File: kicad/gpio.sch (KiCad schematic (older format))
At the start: 11 parts

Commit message: usb interface changed by emu_interface
I've cleaned all the jtag interface, so the only things that go out is
jtag HOT and rx/tx isolated. I left the isolator for rx/tx cose I'm
planning to add rs485 using the same isolator and regulator, if not, I'd
clean these IC's also
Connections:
- net labels added: VDD3V3
- net labels removed: VDD
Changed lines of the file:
@@
 EESchema Schematic File Version 4
-LIBS:servo-cache
 EELAYER 26 0
 EELAYER END
 $Descr B 17000 11000
 encoding utf-8
-Sheet 4 7
+Sheet 3 6
 Title "gpio"
 Date "25 10 2019"
@@
 MCU_GPIO147
 $Comp
-L servo:VDD #PWR0409
+L servo:VDD3V3 #PWR0409
 U 1 1 5DB39007
 P 8050 1700
+AR Path="/5DB39007" Ref="#PWR0409"  Part="1"
+AR Path="/5DE49152/5DB39007" Ref="#PWR0409"  Part="1"
 F 0 "#PWR0409" H 8067 1909 20  0000 C CNN
-F 1 "VDD" H 8067 1857 30  0000 C CNN
+F 1 "VDD3V3" H 8067 1857 30  0000 C CNN
 F 2 "" H 8050 1700 70  0000 C CNN
 F 3 "" H 8050 1700 70  0000 C CNN
@@
 F 1 "~" H 3000 5100 50  0001 C CNN
 F 2 "" H 3000 5100 50  0001 C CNN
-F 3 "" H 3000 5100 50  0001 C CNN
+F 3 "../doc/datasheets/tms320f28388d_datasheet.pdf" H 3000 5100 50  0001 C CNN
 F 4 "TMS320F28388DZWTS" V 1400 2000 60  0001 C CNN "PartNumber"
 	1    3000 5100

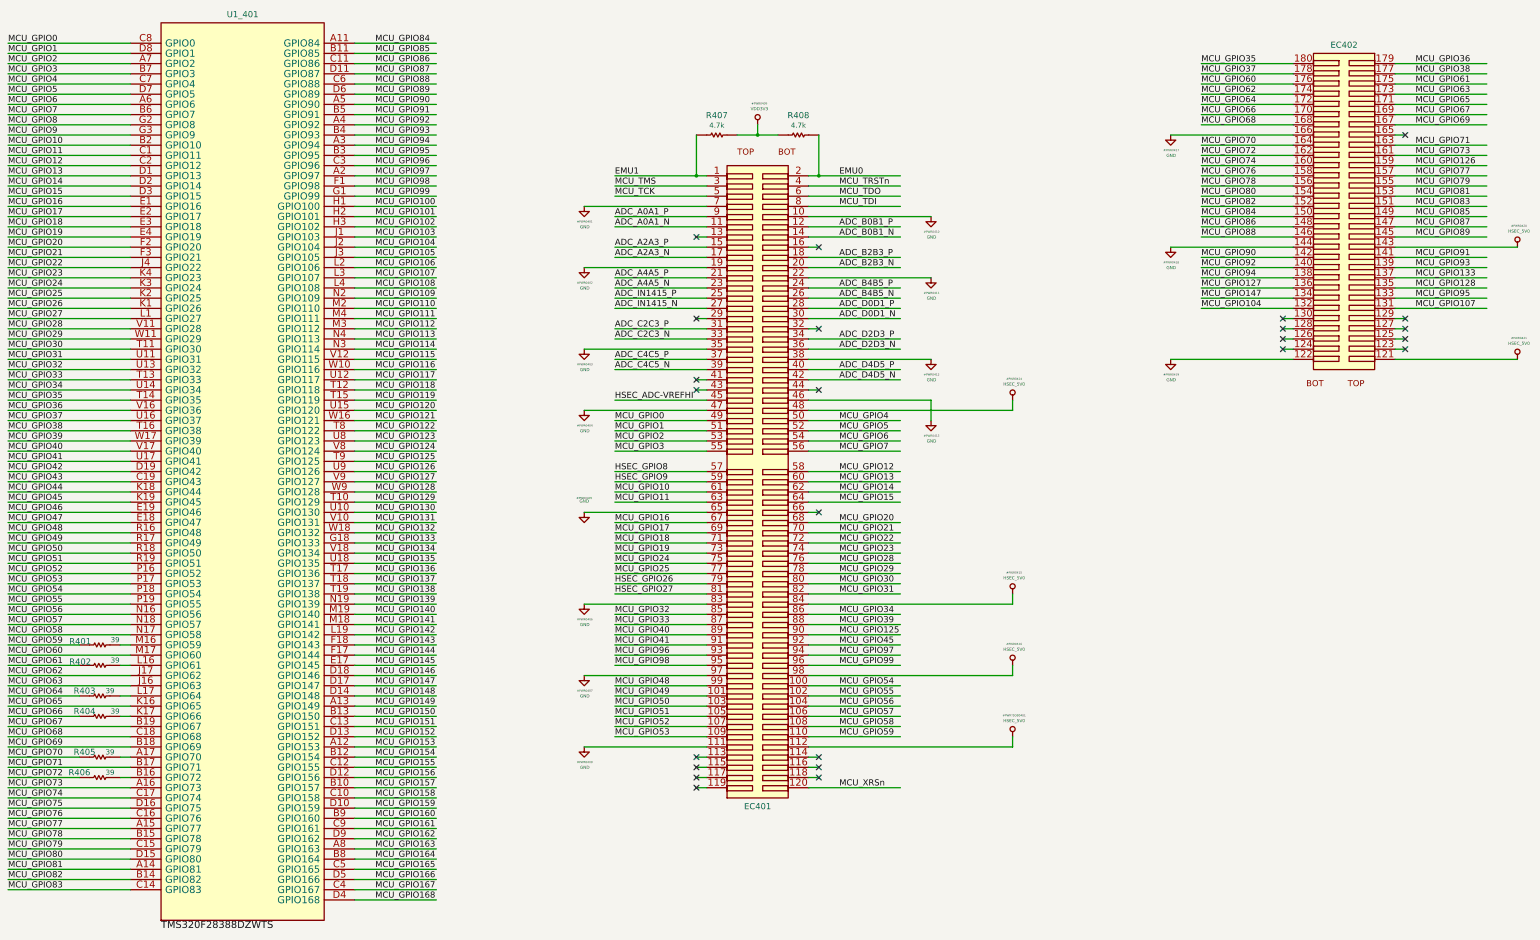
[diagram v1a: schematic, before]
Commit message: power.sch added with new power 1V2, 3V3, an so global labels
I've added the power schematic and try to ojin the power label as 3V3,
VDD_3V3 an so.. keep going
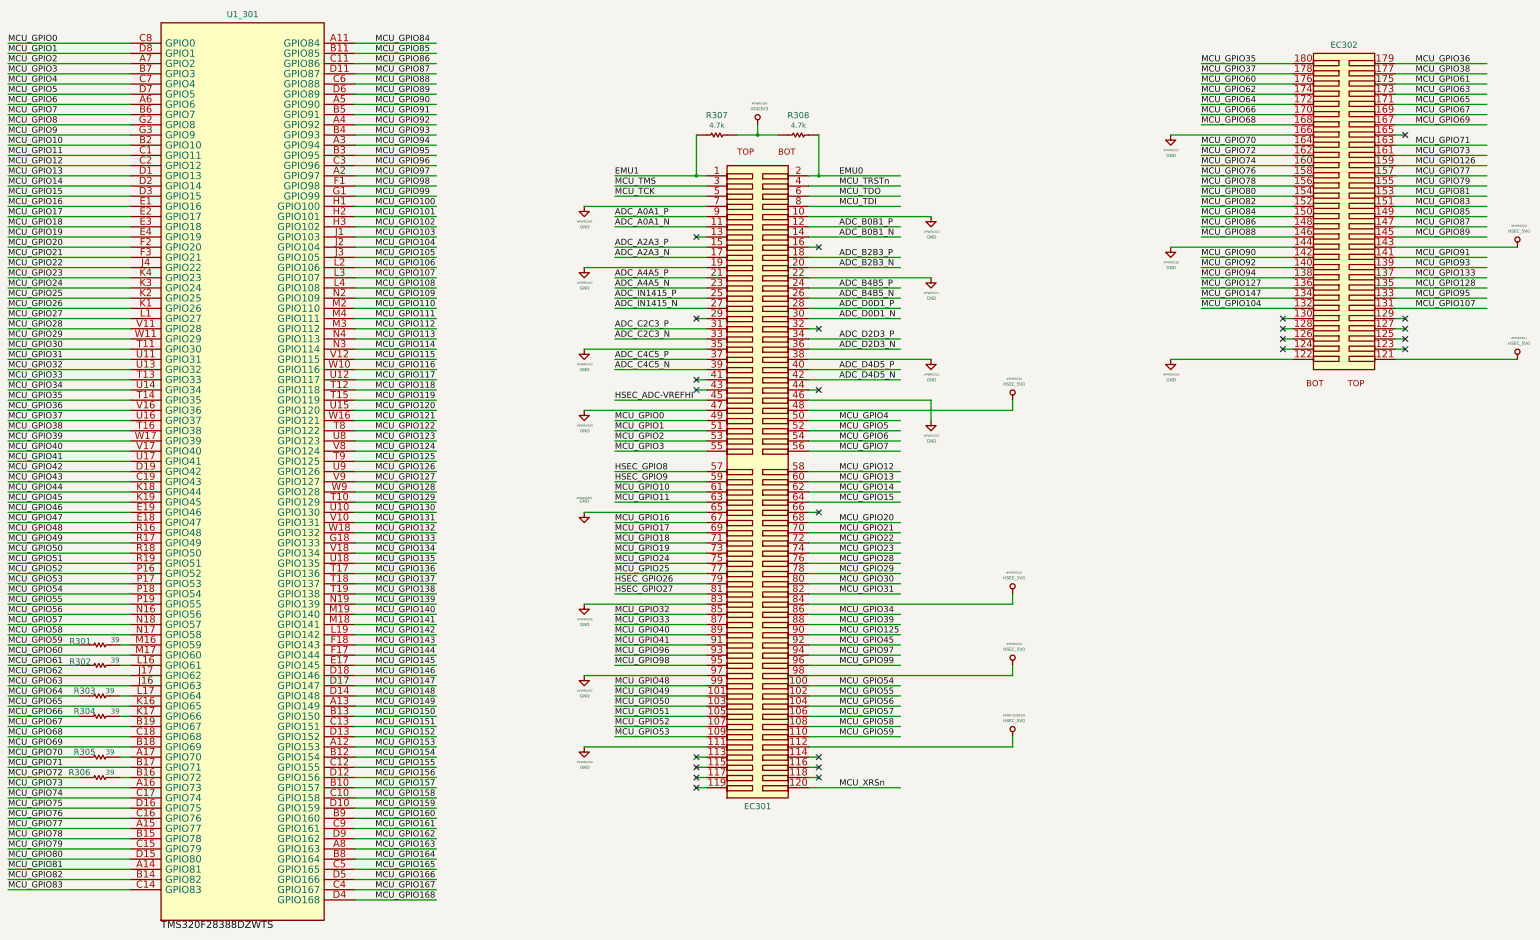
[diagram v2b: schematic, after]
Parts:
- renumbered EC401 to EC301, EC402 to EC302, R401 to R301, R402 to R302, R403 to R303, R404 to R304, R405 to R305, R406 to R306, R407 to R307, R408 to R308, U1_401 to U1_301
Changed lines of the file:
@@
 EESchema Schematic File Version 4
+LIBS:servo-cache
 EELAYER 26 0
 EELAYER END
 $Descr B 17000 11000
 encoding utf-8
-Sheet 3 6
+Sheet 3 7
 Title "gpio"
 Date "25 10 2019"
@@
 $EndDescr
 $Comp
-L servo:GND #PWR0401
+L servo:GND #PWR0301
 U 1 1 5DB3901C
 P 6350 2500
-F 0 "#PWR0401" H 6355 2351 20  0000 C CNN
+F 0 "#PWR0301" H 6355 2351 20  0000 C CNN
 F 1 "GND" H 6355 2299 30  0000 C CNN
 F 2 "" H 6350 2500 70  0000 C CNN
@@
 $EndComp
 $Comp
-L servo:GND #PWR0402
+L servo:GND #PWR0302
 U 1 1 5DB3901B
 P 6350 3100
-F 0 "#PWR0402" H 6355 2951 20  0000 C CNN
+F 0 "#PWR0302" H 6355 2951 20  0000 C CNN
 F 1 "GND" H 6355 2899 30  0000 C CNN
 F 2 "" H 6350 3100 70  0000 C CNN
@@
 $EndComp
 $Comp
-L servo:GND #PWR0403
+L servo:GND #PWR0303
 U 1 1 5DB3901A
 P 6350 3900
-F 0 "#PWR0403" H 6355 3751 20  0000 C CNN
+F 0 "#PWR0303" H 6355 3751 20  0000 C CNN
 F 1 "GND" H 6355 3699 30  0000 C CNN
 F 2 "" H 6350 3900 70  0000 C CNN
@@
 $EndComp
 $Comp
-L servo:GND #PWR0404
+L servo:GND #PWR0304
 U 1 1 5DB39019
 P 6350 4500
-F 0 "#PWR0404" H 6355 4351 20  0000 C CNN
+F 0 "#PWR0304" H 6355 4351 20  0000 C CNN
 F 1 "GND" H 6355 4299 30  0000 C CNN
 F 2 "" H 6350 4500 70  0000 C CNN
@@
 $EndComp
 $Comp
-L servo:GND #PWR0405
+L servo:GND #PWR0305
 U 1 1 5DB39018
 P 6350 5500
-F 0 "#PWR0405" H 6350 5640 20  0000 C CNN
+F 0 "#PWR0305" H 6350 5640 20  0000 C CNN
 F 1 "GND" H 6350 5610 30  0000 C CNN
 F 2 "" H 6350 5500 70  0000 C CNN
@@
 $EndComp
 $Comp
-L servo:GND #PWR0406
+L servo:GND #PWR0306
 U 1 1 5DB39017
 P 6350 6400
-F 0 "#PWR0406" H 6355 6251 20  0000 C CNN
+F 0 "#PWR0306" H 6355 6251 20  0000 C CNN
 F 1 "GND" H 6355 6199 30  0000 C CNN
 F 2 "" H 6350 6400 70  0000 C CNN
@@
 $EndComp
 $Comp
-L servo:GND #PWR0407
+L servo:GND #PWR0307
 U 1 1 5DB39016
 P 6350 7100
-F 0 "#PWR0407" H 6355 6951 20  0000 C CNN
+F 0 "#PWR0307" H 6355 6951 20  0000 C CNN
 F 1 "GND" H 6355 6899 30  0000 C CNN
 F 2 "" H 6350 7100 70  0000 C CNN
@@
 $EndComp
 $Comp
-L servo:GND #PWR0408
+L servo:GND #PWR0308
 U 1 1 5DB39015
 P 6350 7800
-F 0 "#PWR0408" H 6355 7651 20  0000 C CNN
+F 0 "#PWR0308" H 6355 7651 20  0000 C CNN
 F 1 "GND" H 6355 7599 30  0000 C CNN
 F 2 "" H 6350 7800 70  0000 C CNN
@@
 $EndComp
 $Comp
-L servo:GND #PWR0410
+L servo:GND #PWR0310
 U 1 1 5DB39014
 P 9750 2600
-F 0 "#PWR0410" H 9755 2451 20  0000 C CNN
+F 0 "#PWR0310" H 9755 2451 20  0000 C CNN
 F 1 "GND" H 9755 2399 30  0000 C CNN
 F 2 "" H 9750 2600 70  0000 C CNN
@@
 $EndComp
 $Comp
-L servo:GND #PWR0411
+L servo:GND #PWR0311
 U 1 1 5DB39013
 P 9750 3200
-F 0 "#PWR0411" H 9755 3051 20  0000 C CNN
+F 0 "#PWR0311" H 9755 3051 20  0000 C CNN
 F 1 "GND" H 9755 2999 30  0000 C CNN
 F 2 "" H 9750 3200 70  0000 C CNN
@@
 $EndComp
 $Comp
-L servo:GND #PWR0412
+L servo:GND #PWR0312
 U 1 1 5DB39012
 P 9750 4000
-F 0 "#PWR0412" H 9755 3851 20  0000 C CNN
+F 0 "#PWR0312" H 9755 3851 20  0000 C CNN
 F 1 "GND" H 9755 3799 30  0000 C CNN
 F 2 "" H 9750 4000 70  0000 C CNN
@@
 $EndComp
 $Comp
-L servo:GND #PWR0413
+L servo:GND #PWR0313
 U 1 1 5DB39011
 P 9750 4600
-F 0 "#PWR0413" H 9755 4451 20  0000 C CNN
+F 0 "#PWR0313" H 9755 4451 20  0000 C CNN
 F 1 "GND" H 9755 4399 30  0000 C CNN
 F 2 "" H 9750 4600 70  0000 C CNN
@@
 MCU_GPIO9
 $Comp
-L servo:GND #PWR0417
+L servo:GND #PWR0317
 U 1 1 5DB39010
 P 12100 1800
-F 0 "#PWR0417" H 12105 1651 20  0000 C CNN
+F 0 "#PWR0317" H 12105 1651 20  0000 C CNN
 F 1 "GND" H 12105 1599 30  0000 C CNN
 F 2 "" H 12100 1800 70  0000 C CNN
@@
 $EndComp
 $Comp
-L servo:GND #PWR0418
+L servo:GND #PWR0318
 U 1 1 5DB3900F
 P 12100 2900
-F 0 "#PWR0418" H 12105 2751 20  0000 C CNN
+F 0 "#PWR0318" H 12105 2751 20  0000 C CNN
 F 1 "GND" H 12105 2699 30  0000 C CNN
 F 2 "" H 12100 2900 70  0000 C CNN
@@
 $EndComp
 $Comp
-L servo:GND #PWR0419
+L servo:GND #PWR0319
 U 1 1 5DB3900E
 P 12100 4000
-F 0 "#PWR0419" H 12105 3851 20  0000 C CNN
+F 0 "#PWR0319" H 12105 3851 20  0000 C CNN
 F 1 "GND" H 12105 3799 30  0000 C CNN
 F 2 "" H 12100 4000 70  0000 C CNN
@@
 	15500 2900 14300 2900
 $Comp
-L servo:HSEC_5V0 #PWR0420
+L servo:HSEC_5V0 #PWR0320
 U 1 1 5DB3900D
 P 15500 2900
-F 0 "#PWR0420" H 15515 3109 20  0000 C CNN
+F 0 "#PWR0320" H 15515 3109 20  0000 C CNN
 F 1 "HSEC_5V0" H 15515 3057 30  0000 C CNN
 F 2 "" H 15500 2900 70  0000 C CNN
@@
 $EndComp
 $Comp
-L servo:HSEC_5V0 #PWR0421
+L servo:HSEC_5V0 #PWR0321
 U 1 1 5DB3900C
 P 15500 4000
-F 0 "#PWR0421" H 15515 4209 20  0000 C CNN
+F 0 "#PWR0321" H 15515 4209 20  0000 C CNN
 F 1 "HSEC_5V0" H 15515 4157 30  0000 C CNN
 F 2 "" H 15500 4000 70  0000 C CNN
@@
 	10550 4400 10550 4500
 $Comp
-L servo:HSEC_5V0 #PWR0414
+L servo:HSEC_5V0 #PWR0314
 U 1 1 5DB3900B
 P 10550 4400
-F 0 "#PWR0414" H 10565 4609 20  0000 C CNN
+F 0 "#PWR0314" H 10565 4609 20  0000 C CNN
 F 1 "HSEC_5V0" H 10565 4557 30  0000 C CNN
 F 2 "" H 10550 4400 70  0000 C CNN
@@
 $EndComp
 $Comp
-L servo:HSEC_5V0 #PWR0415
+L servo:HSEC_5V0 #PWR0315
 U 1 1 5DB3900A
 P 10550 6300
-F 0 "#PWR0415" H 10565 6509 20  0000 C CNN
+F 0 "#PWR0315" H 10565 6509 20  0000 C CNN
 F 1 "HSEC_5V0" H 10565 6457 30  0000 C CNN
 F 2 "" H 10550 6300 70  0000 C CNN
@@
 	10550 7000 10550 7100
 $Comp
-L servo:HSEC_5V0 #PWR0416
+L servo:HSEC_5V0 #PWR0316
 U 1 1 5DB39009
 P 10550 7000
-F 0 "#PWR0416" H 10565 7209 20  0000 C CNN
+F 0 "#PWR0316" H 10565 7209 20  0000 C CNN
 F 1 "HSEC_5V0" H 10565 7157 30  0000 C CNN
 F 2 "" H 10550 7000 70  0000 C CNN
@@
 	10550 7700 10550 7800
 $Comp
-L servo:HSEC_5V0 #PWR?5DB0401
+L servo:HSEC_5V0 #PWR?5DB0301
 U 1 1 5DB39008
 P 10550 7700
-F 0 "#PWR?5DB0401" H 10565 7909 20  0000 C CNN
+F 0 "#PWR?5DB0301" H 10565 7909 20  0000 C CNN
 F 1 "HSEC_5V0" H 10565 7857 30  0000 C CNN
 F 2 "" H 10550 7700 70  0000 C CNN
@@
 MCU_GPIO147
 $Comp
-L servo:VDD3V3 #PWR0409
+L servo:VDD_3V3 #PWR?
 U 1 1 5DB39007
 P 8050 1700
-AR Path="/5DB39007" Ref="#PWR0409"  Part="1"
-AR Path="/5DE49152/5DB39007" Ref="#PWR0409"  Part="1"
-F 0 "#PWR0409" H 8067 1909 20  0000 C CNN
+AR Path="/5DB39007" Ref="#PWR?"  Part="1"
+AR Path="/5DE49152/5DB39007" Ref="#PWR0309"  Part="1"
+F 0 "#PWR0309" H 8067 1909 20  0000 C CNN
 F 1 "VDD3V3" H 8067 1857 30  0000 C CNN
 F 2 "" H 8050 1700 70  0000 C CNN
@@
 Connection ~ 8650 2200
 $Comp
-L servo:controlCARD-120HSEC_Edge EC401
+L servo:controlCARD-120HSEC_Edge EC301
 U 1 1 5DB39006
 P 8050 5200
-F 0 "EC401" H 8050 2017 60  0000 C CNN
+F 0 "EC301" H 8050 2017 60  0000 C CNN
 F 1 "~" H 8050 5200 50  0001 C CNN
 F 2 "" H 8050 5200 50  0001 C CNN
@@
 $EndComp
 $Comp
-L servo:Resistor R407
+L servo:Resistor R307
 U 1 1 5DB39005
 P 7650 1800
-F 0 "R407" H 7650 1993 60  0000 C CNN
+F 0 "R307" H 7650 1993 60  0000 C CNN
 F 1 "4.7k" H 7650 1895 50  0000 C CNN
 F 2 "" H 7650 1800 50  0001 C CNN
@@
 $EndComp
 $Comp
-L servo:Resistor R408
+L servo:Resistor R308
 U 1 1 5DB39004
 P 8450 1800
-F 0 "R408" H 8450 1993 60  0000 C CNN
+F 0 "R308" H 8450 1993 60  0000 C CNN
 F 1 "4.7k" H 8450 1895 50  0000 C CNN
 F 2 "" H 8450 1800 50  0001 C CNN
@@
 $EndComp
 $Comp
-L servo:controlCARD-180HSEC-60pinAddon_Edge EC402
+L servo:controlCARD-180HSEC-60pinAddon_Edge EC302
 U 1 1 5DB39003
 P 13800 2500
-F 0 "EC402" H 13800 917 60  0000 C CNN
+F 0 "EC302" H 13800 917 60  0000 C CNN
 F 1 "~" H 13800 2500 50  0001 C CNN
 F 2 "" H 13800 2500 50  0001 C CNN
@@
 $EndComp
 $Comp
-L servo:Resistor R403
+L servo:Resistor R303
 U 1 1 5DB39002
 P 1600 7300
-F 0 "R403" H 1450 7350 60  0000 C CNN
+F 0 "R303" H 1450 7350 60  0000 C CNN
 F 1 "39" H 1700 7350 50  0000 C CNN
 F 2 "" H 1600 7300 50  0001 C CNN
@@
 $EndComp
 $Comp
-L servo:Resistor R401
+L servo:Resistor R301
 U 1 1 5DB39001
 P 1600 6800
-F 0 "R401" H 1300 6800 60  0000 L BNN
+F 0 "R301" H 1300 6800 60  0000 L BNN
 F 1 "39" H 1750 6850 50  0000 C CNN
 F 2 "" H 1600 6800 50  0001 C CNN
@@
 $EndComp
 $Comp
-L servo:Resistor R402
+L servo:Resistor R302
 U 1 1 5DB39000
 P 1600 7000
-F 0 "R402" H 1300 7000 60  0000 L BNN
+F 0 "R302" H 1300 7000 60  0000 L BNN
 F 1 "39" H 1750 7050 50  0000 C CNN
 F 2 "" H 1600 7000 50  0001 C CNN
@@
 $EndComp
 $Comp
-L servo:Resistor R404
+L servo:Resistor R304
 U 1 1 5DB38FFF
 P 1600 7500
-F 0 "R404" H 1450 7550 60  0000 C CNN
+F 0 "R304" H 1450 7550 60  0000 C CNN
 F 1 "39" H 1750 7550 50  0000 C CNN
 F 2 "" H 1600 7500 50  0001 C CNN
@@
 $EndComp
 $Comp
-L servo:Resistor R405
+L servo:Resistor R305
 U 1 1 5DB38FFE
 P 1600 7900
-F 0 "R405" H 1450 7950 60  0000 C CNN
+F 0 "R305" H 1450 7950 60  0000 C CNN
 F 1 "39" H 1700 7950 50  0000 C CNN
 F 2 "" H 1600 7900 50  0001 C CNN
@@
 $EndComp
 $Comp
-L servo:Resistor R406
+L servo:Resistor R306
 U 1 1 5DB38FFD
 P 1600 8100
-F 0 "R406" H 1400 8150 60  0000 C CNN
+F 0 "R306" H 1400 8150 60  0000 C CNN
 F 1 "39" H 1700 8150 50  0000 C CNN
 F 2 "" H 1600 8100 50  0001 C CNN
@@
 $EndComp
 $Comp
-L servo:TMS320F28388_2 U1_401
+L servo:TMS320F28388_2 U1_301
 U 1 1 5DB38FFC
 P 3000 5100
-F 0 "U1_401" H 3000 9583 60  0000 C CNN
+F 0 "U1_301" H 3000 9583 60  0000 C CNN
 F 1 "~" H 3000 5100 50  0001 C CNN
 F 2 "" H 3000 5100 50  0001 C CNN

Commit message: cleaning power, added ac/dc to 15v
I've added the ac/dc power supply based on encapsulated off load power
supply and chainde linear regulator for 5, 3v3 and 1v2 for cold gnd and
5v and 3v3 for hot gnd.
I'll next join some sheet 'cose some of those are almost empty
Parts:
- removed EC301: ~, symbol servo:controlCARD-120HSEC_Edge
- removed EC302: ~, symbol servo:controlCARD-180HSEC-60pinAddon_Edge
- removed R307, R308: 4.7k, symbol servo:Resistor
- U1_301: value ~ -> TMS320F28388DZWTS; symbol servo:TMS320F28388_2 -> servo:TMS320F28388
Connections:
- net labels removed: ADC_A0A1_N, ADC_A0A1_P, ADC_A2A3_N, ADC_A2A3_P, ADC_A4A5_N, ADC_A4A5_P, ADC_B0B1_N, ADC_B0B1_P, ADC_B2B3_N, ADC_B2B3_P, ADC_B4B5_N, ADC_B4B5_P, ADC_C2C3_N, ADC_C2C3_P, ADC_C4C5_N, ADC_C4C5_P, ADC_D0D1_N, ADC_D0D1_P, ADC_D2D3_N, ADC_D2D3_P, ADC_D4D5_N, ADC_D4D5_P, ADC_IN1415_N, ADC_IN1415_P, EMU0, EMU1, GND, HSEC_5V0, HSEC_ADC-VREFHI, HSEC_GPIO26, HSEC_GPIO27, HSEC_GPIO8, HSEC_GPIO9, MCU_TCK, MCU_TDI, MCU_TDO, MCU_TMS, MCU_TRSTn, MCU_XRSn, TMS320F28388DZWTS, VDD3V3
- wire segments 367 -> 175
- no-connect marks 24 -> 0
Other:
- moved on the sheet: R301, R302, R303, R304, R305, R306

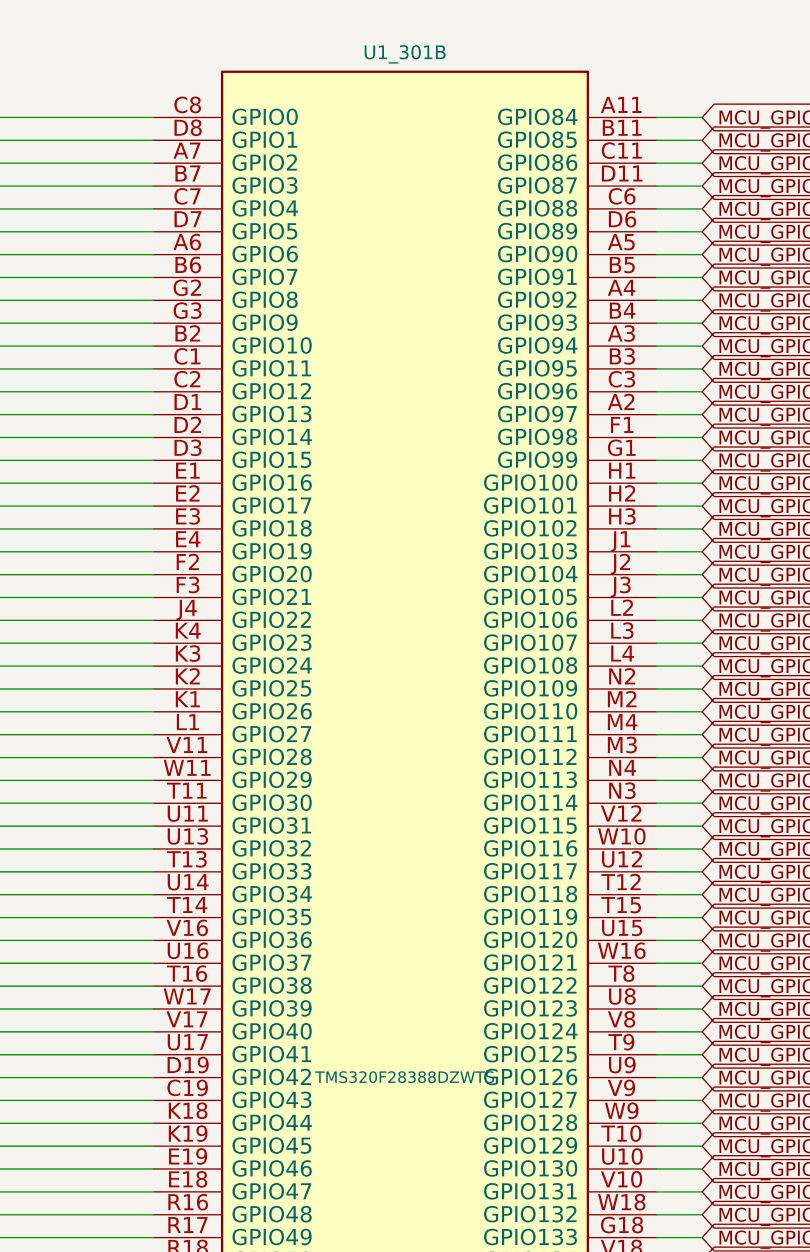
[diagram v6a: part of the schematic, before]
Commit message: added igbt interface, lem, and impprove root page
improved root page, added lem using hall sensor instead shunt, add
somthing on adc page, and ac input.. keep working
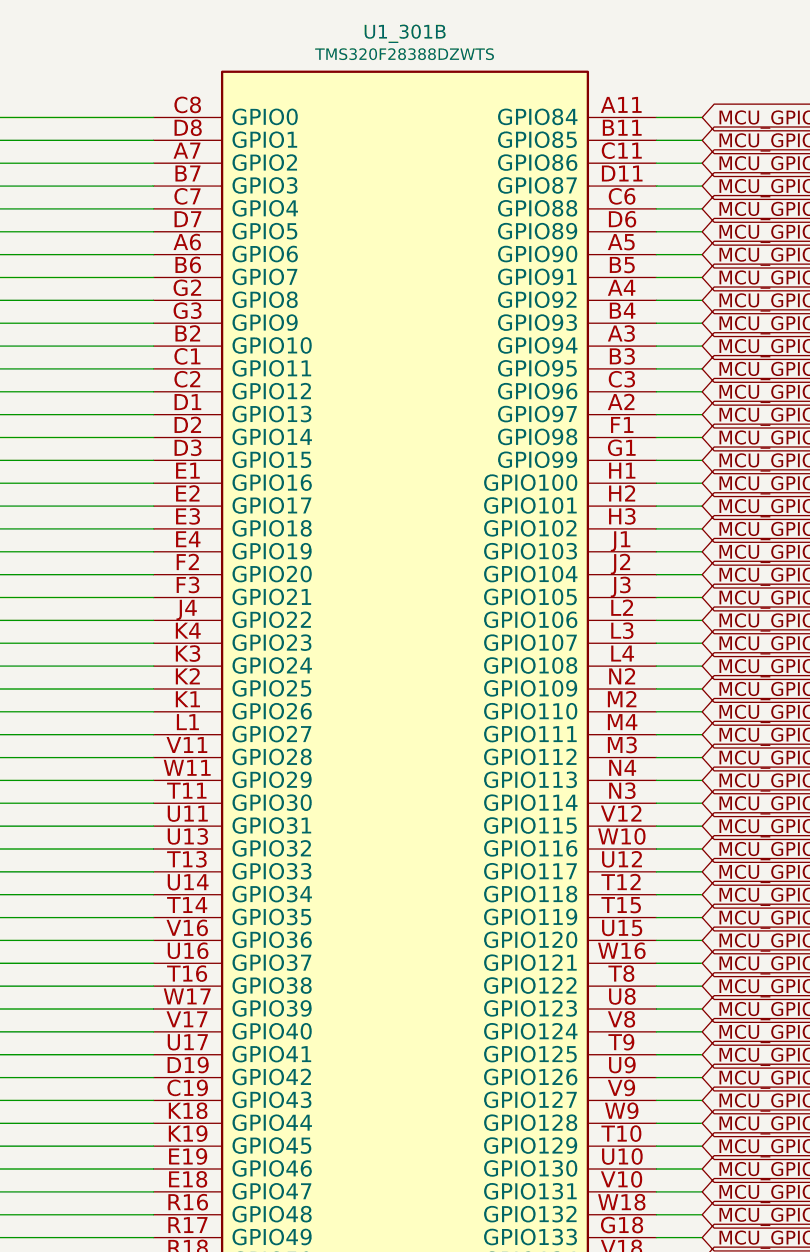
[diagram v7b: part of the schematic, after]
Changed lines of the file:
@@
 EESchema Schematic File Version 4
+LIBS:servo-cache
 EELAYER 26 0
 EELAYER END
 $Descr B 17000 11000
 encoding utf-8
-Sheet 3 9
+Sheet 10 10
 Title "gpio"
 Date "25 10 2019"
@@
 U 2 1 5DB38FFC
 P 5550 5200
-F 0 "U1_301" H 5550 9683 60  0000 C CNN
-F 1 "TMS320F28388DZWTS" H 5550 5200 50  0000 C CNN
+F 0 "U1_301" H 5550 9773 60  0000 C CNN
+F 1 "TMS320F28388DZWTS" H 5550 9675 50  0000 C CNN
 F 2 "" H 5550 5200 50  0001 C CNN
 F 3 "../doc/datasheets/tms320f28388d_datasheet.pdf" H 5550 5200 50  0001 C CNN
